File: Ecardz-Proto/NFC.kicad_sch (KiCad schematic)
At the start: 8 parts, among them IC1 M24LR04E-RDW6T_2

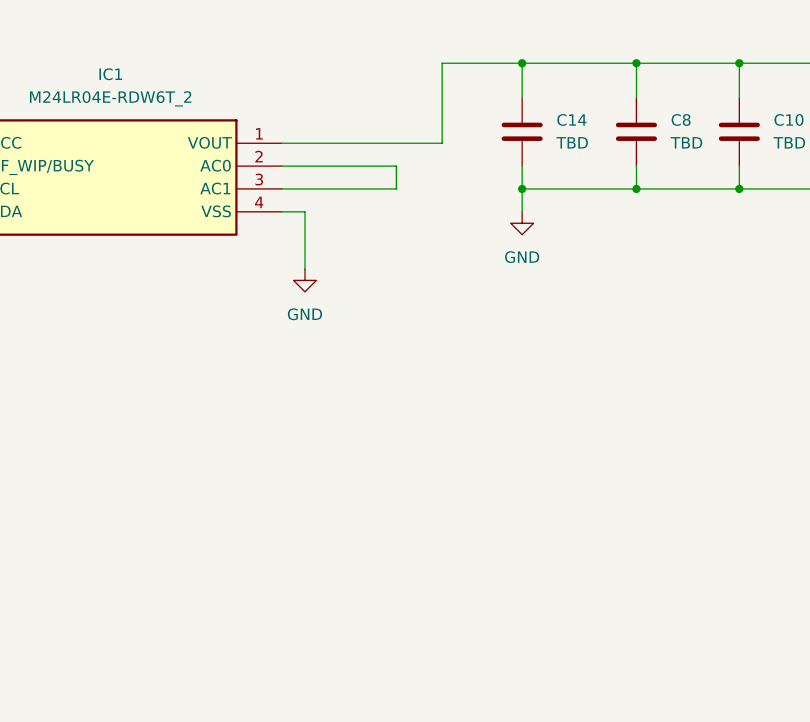
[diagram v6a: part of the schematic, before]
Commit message: added antenna tuning caps
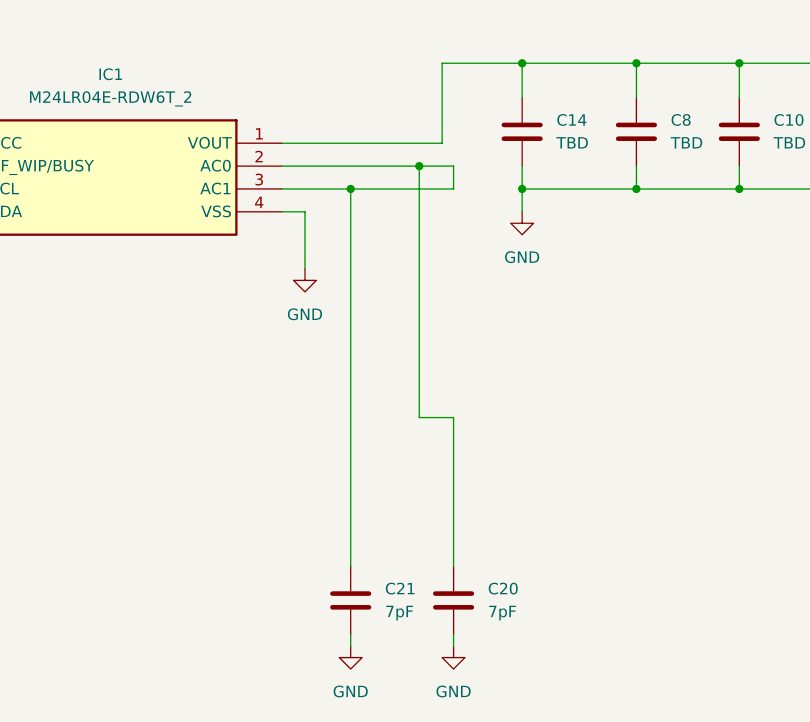
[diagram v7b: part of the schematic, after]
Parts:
- added C20, C21: 7pF, Capacitor_SMD:C_0201_0603Metric_Pad0.64x0.40mm_HandSolder, symbol Device:C
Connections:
- net GND: now also C20.2, C21.2
- net at IC1.2 (AC0), IC1.3 (AC1): now also C20.1, C21.1

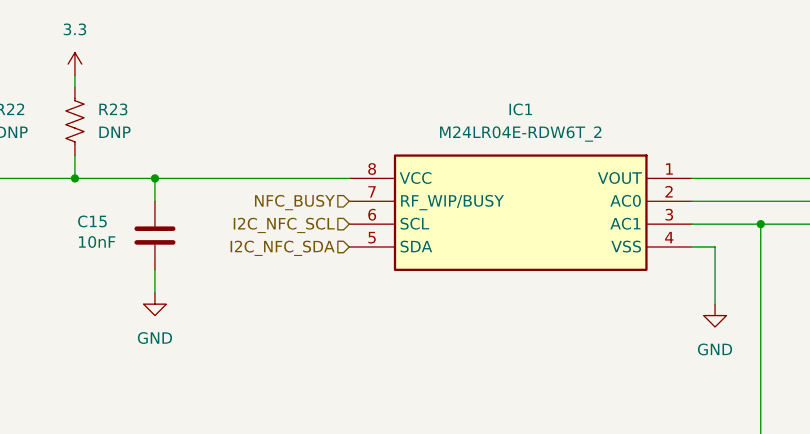
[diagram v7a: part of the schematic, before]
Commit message: rough layout complete
need to fix silkscreens and finish antenna
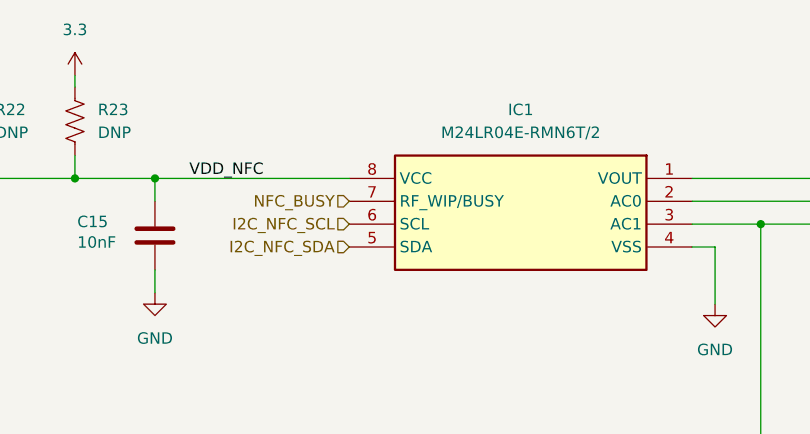
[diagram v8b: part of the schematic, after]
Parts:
- IC1: value M24LR04E-RDW6T_2 -> M24LR04E-RMN6T/2; footprint SOP65P640X120-8N -> Package_SO:SO-8_3.9x4.9mm_P1.27mm
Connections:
- net VDD_NFC: now reaches C15.1, IC1.8 (VCC), R22.1, R23.1
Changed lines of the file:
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@@
+		)
+	)
+	(label "VDD_NFC"
+		(at 121.92 34.29 0)
+		(fields_autoplaced yes)
+		(effects
+			(font
+				(size 1.27 1.27)
+			)
+			(justify left bottom)
 		)
 	)
@@
 			)
 		)
-		(property "Value" "M24LR04E-RDW6T_2"
+		(property "Value" "M24LR04E-RMN6T/2"
 			(at 158.75 29.21 0)
 			(effects
@@
 			)
 		)
-		(property "Footprint" "SOP65P640X120-8N"
+		(property "Footprint" "Package_SO:SO-8_3.9x4.9mm_P1.27mm"
 			(at 143.51 129.21 0)
 			(effects
